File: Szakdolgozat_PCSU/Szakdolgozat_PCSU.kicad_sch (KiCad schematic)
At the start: 66 parts, among them IC1 DRV8244SQDGQRQ1, IC2 TPS54628DDAR, IC3 DRV8244SQDGQRQ1, IC4 LTC4365ITS8-1#TRPBF, J1 MOTOR1_OUT, J2 M1_SPI, J3 M1_CTRL, J4 MOTOR2_OUT, J5 M2_SPI, J6 M2_CTRL, J7 5V_CON, J8 BAT_CON, Q1 STP130N6F7, Q2 STP130N6F7

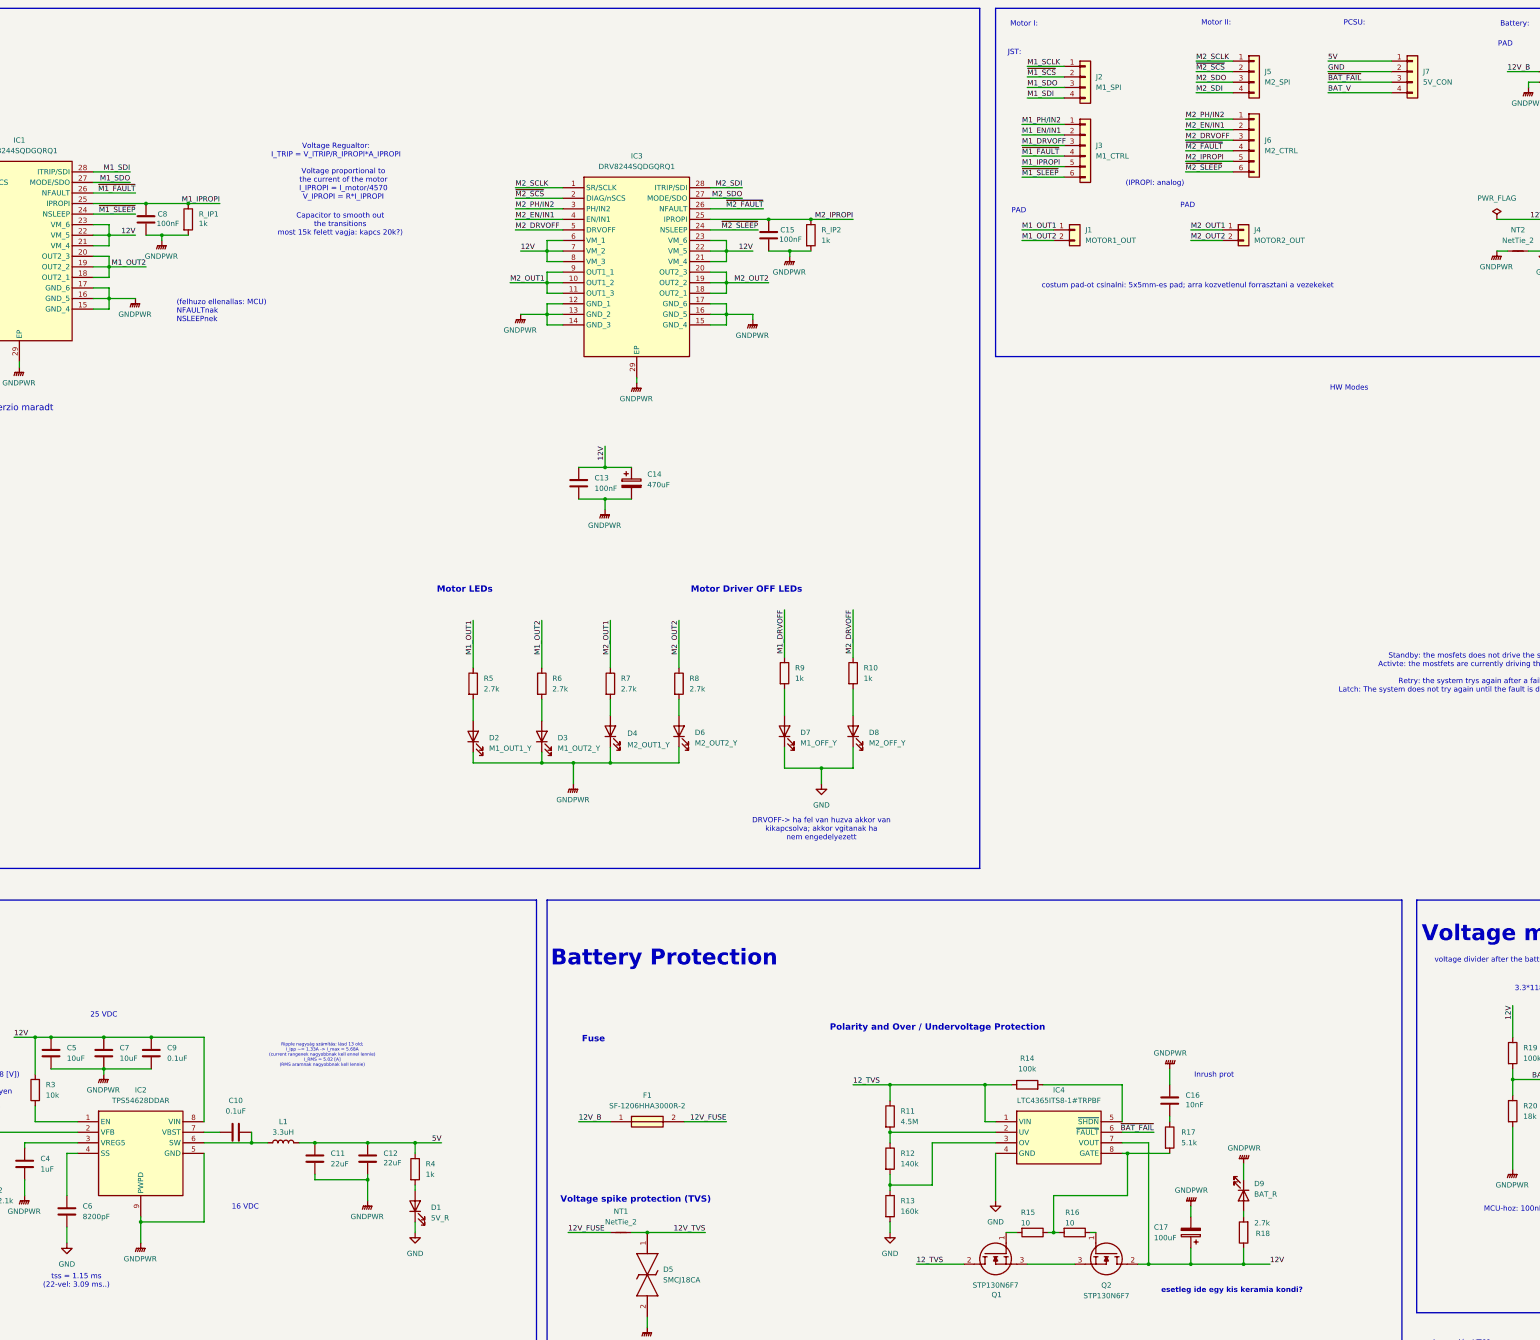
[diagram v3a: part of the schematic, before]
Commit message: Update PCSU PCB routing, copper pours and vias
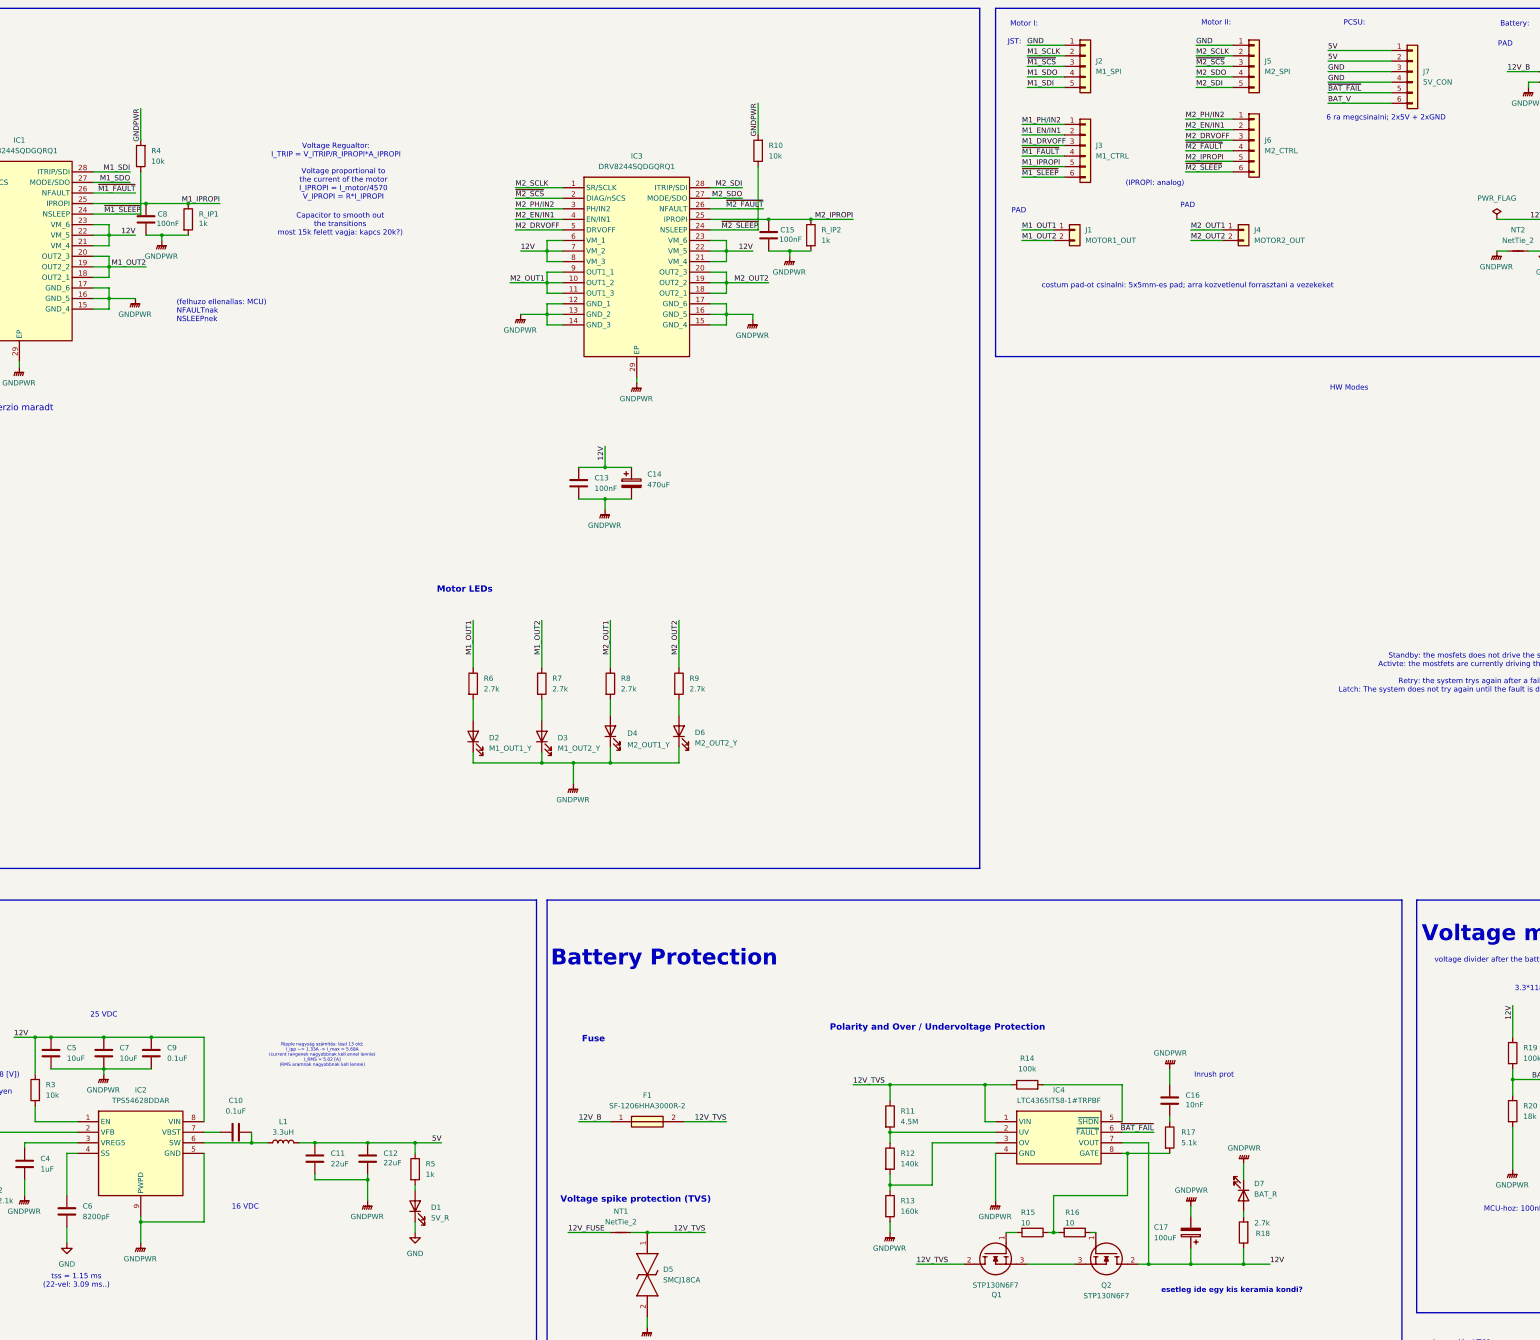
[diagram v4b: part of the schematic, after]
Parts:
- removed D7: M1_OFF_Y, LED_SMD:LED_0603_1608Metric_Pad1.05x0.95mm_HandSolder, symbol Device:LED
- removed D8: M2_OFF_Y, LED_SMD:LED_0603_1608Metric_Pad1.05x0.95mm_HandSolder, symbol Device:LED
- removed R9: 1k, Resistor_SMD:R_0603_1608Metric_Pad0.98x0.95mm_HandSolder, symbol Device:R
- added R4: 10k, Resistor_SMD:R_0603_1608Metric_Pad0.98x0.95mm_HandSolder, symbol Device:R
- C16: footprint Capacitor_SMD:C_1206_3216Metric_Pad1.33x1.80mm_HandSolder -> Capacitor_SMD:C_0603_1608Metric_Pad1.08x0.95mm_HandSolder
- J2, J5: footprint Connector_JST:JST_XH_S4B-XH-A-1_1x04_P2.50mm_Horizontal -> Connector_JST:JST_XH_S5B-XH-A-1_1x05_P2.50mm_Horizontal; symbol Connector_Generic:Conn_01x04 -> Connector_Generic:Conn_01x05
- J7: footprint Connector_JST:JST_XH_S4B-XH-A-1_1x04_P2.50mm_Horizontal -> Connector_JST:JST_XH_S6B-XH-A-1_1x06_P2.50mm_Horizontal; symbol Connector_Generic:Conn_01x04 -> Connector_Generic:Conn_01x06
- NT2: footprint (none) -> NetTie:Untitled; now in the parts list
- R10: value 1k -> 10k
- renumbered D9 to D7, R4 to R5, R5 to R6, R6 to R7, R7 to R8, R8 to R9
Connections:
- net 12_TVS is gone; now on net 12V_TVS: IC4.1 (VIN), Q1.2 (D), R11.1, R14.1
- net 12V_FUSE: no longer F1.2
- net 12V_TVS: now also F1.2
- net 5V: now also J7.2 (Pin_2)
- net BAT_V: now also J7.6 (Pin_6); no longer J7.4 (Pin_4)
- net GND: now also J2.1 (Pin_1), J5.1 (Pin_1), J7.3 (Pin_3), J7.4 (Pin_4); no longer IC4.4 (GND), J7.2 (Pin_2), R13.2
- net GNDPWR: now also IC4.4 (GND), R10.2, R13.2, R4.2
- net M1_SCLK: now also J2.2 (Pin_2); no longer J2.1 (Pin_1)
- net M1_SDI: now also J2.5 (Pin_5); no longer J2.4 (Pin_4)
- net M1_SDO: now also J2.4 (Pin_4); no longer J2.3 (Pin_3)
- net M2_DRVOFF: no longer R10.1
- net M2_SCLK: now also J5.2 (Pin_2); no longer J5.1 (Pin_1)
- net M2_SDI: now also J5.5 (Pin_5); no longer J5.4 (Pin_4)
- net M2_SDO: now also J5.4 (Pin_4); no longer J5.3 (Pin_3)
- net ~{BAT_FAIL}: now also J7.5 (Pin_5); no longer J7.3 (Pin_3)
- net ~{M1_SCS}: now also J2.3 (Pin_3); no longer J2.2 (Pin_2)
- net ~{M1_SLEEP}: now also R4.1
- net ~{M2_SCS}: now also J5.3 (Pin_3); no longer J5.2 (Pin_2)
- net ~{M2_SLEEP}: now also R10.1
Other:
- note added: "6 ra megcsinalni; 2x5V + 2xGND"
- note removed: "DRVOFF-> ha fel van huzva akkor van kikapcsolva; akkor vgitanak ha nem engedelyezett"
- note removed: "Motor Driver OFF LEDs"

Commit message: CU es PCSU Rev A finished + Production Files
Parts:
- removed NT1: NetTie_2, symbol Device:NetTie_2
- C16: Link https://hu.mouser.com/en/ProductDetail/Murata-Electronics/G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 -> https://hu.mouser.com/ProductDetail/Murata-Electronics/GRM1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
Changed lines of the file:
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@@
 	)
 	(junction
-		(at 247.65 309.88)
-		(diameter 0)
-		(color 0 0 0 0)
-	)
-	(junction
 		(at 223.52 73.66)
 		(diameter 0)
@@
 	(wire
 		(pts
-			(xy 247.65 309.88) (xy 261.62 309.88)
-		)
-		(stroke
-			(width 0)
-			(type default)
-		)
-	)
-	(wire
-		(pts
 			(xy 361.95 290.83) (xy 363.22 290.83)
 		)
@@
 	(wire
 		(pts
-			(xy 228.6 309.88) (xy 238.76 309.88)
-		)
-		(stroke
-			(width 0)
-			(type default)
-		)
-	)
-	(wire
-		(pts
 			(xy 266.7 73.66) (xy 266.7 76.2)
 		)
@@
 	(wire
 		(pts
-			(xy 243.84 309.88) (xy 247.65 309.88)
-		)
-		(stroke
-			(width 0)
-			(type default)
-		)
-	)
-	(wire
-		(pts
 			(xy 306.07 307.34) (xy 306.07 309.88)
 		)
@@
 		)
 	)
-	(label "12V_TVS"
-		(at 261.62 309.88 180)
-		(effects
-			(font
-				(size 1.27 1.27)
-			)
-			(justify right bottom)
-		)
-	)
 	(label "M1_EN{slash}IN1"
 		(at 337.82 45.72 0)
@@
 		)
 	)
-	(label "12V_FUSE"
-		(at 228.6 309.88 0)
-		(effects
-			(font
-				(size 1.27 1.27)
-			)
-			(justify left bottom)
-		)
-	)
 	(label "M1_OUT2"
 		(at 337.82 71.12 0)
@@
 	)
 	(symbol
-		(lib_id "Device:NetTie_2")
-		(at 241.3 309.88 0)
-		(unit 1)
-		(body_style 1)
-		(exclude_from_sim no)
-		(in_bom no)
-		(on_board yes)
-		(in_pos_files yes)
-		(dnp no)
-		(fields_autoplaced yes)
-		(property "Reference" "NT1"
-			(at 241.3 304.8 0)
-			(show_name no)
-			(do_not_autoplace no)
-			(effects
-				(font
-					(size 1.27 1.27)
-				)
-			)
-		)
-		(property "Value" "NetTie_2"
-			(at 241.3 307.34 0)
-			(show_name no)
-			(do_not_autoplace no)
-			(effects
-				(font
-					(size 1.27 1.27)
-				)
-			)
-		)
-		(property "Footprint" ""
-			(at 241.3 309.88 0)
-			(hide yes)
-			(show_name no)
-			(do_not_autoplace no)
-			(effects
-				(font
-					(size 1.27 1.27)
-				)
-			)
-		)
-		(property "Datasheet" ""
-			(at 241.3 309.88 0)
-			(hide yes)
-			(show_name no)
-			(do_not_autoplace no)
-			(effects
-				(font
-					(size 1.27 1.27)
-				)
-			)
-		)
-		(property "Description" "Net tie, 2 pins"
-			(at 241.3 309.88 0)
-			(hide yes)
-			(show_name no)
-			(do_not_autoplace no)
-			(effects
-				(font
-					(size 1.27 1.27)
-				)
-			)
-		)
-		(pin "2"
-		)
-		(pin "1"
-		)
-		(instances
-			(project "Szakdolgozat_PCSU"
-				(path "/7dedd975-a421-4fd7-bcb8-a9f9c9e19d4a"
-					(reference "NT1")
-					(unit 1)
-				)
-			)
-		)
-	)
-	(symbol
 		(lib_id "power:GNDPWR")
 		(at 459.74 34.29 0)
@@
 			)
 		)
-		(property "Datasheet" "https://hu.mouser.com/datasheet/3/76/4/GRM319R61C226KE15_04A.pdf"
+		(property "Datasheet" "https://search.murata.co.jp/Ceramy/image/img/A01X/G101/ENG/GRM188R71H103KA01-01.pdf"
 			(at 373.38 278.13 0)
 			(hide yes)
@@
 			)
 		)
-		(property "Link" "https://hu.mouser.com/en/ProductDetail/Murata-Electronics/GRM319R61C226KE15D?qs=eeBpzGFlv%252B%252BgKZpdhYn80g%3D%3D"
+		(property "Link" "https://hu.mouser.com/ProductDetail/Murata-Electronics/GRM188R71H103KA01D"
 			(at 373.38 278.13 0)
 			(hide yes)
@@
 	)
 	(embedded_fonts no)
+(symbol
+		(lib_id "power:PWR_FLAG")
+		(at 64.77 139.7 0)
+		(unit 1)
+		(body_style 1)
+		(exclude_from_sim no)
+		(in_bom yes)
+		(on_board yes)
+		(in_pos_files yes)
+		(dnp no)
+		(fields_autoplaced yes)
+		(property "Reference" "#FLG02"
+			(at 64.77 137.795 0)
+			(hide yes)
+			(show_name no)
+			(do_not_autoplace no)
+			(effects
+				(font
+					(size 1.27 1.27)
+				)
+			)
+		)
+		(property "Value" "PWR_FLAG"
+			(at 64.77 134.62 0)
+			(show_name no)
+			(do_not_autoplace no)
+			(effects
+				(font
+					(size 1.27 1.27)
+				)
+			)
+		)
+		(property "Footprint" ""
+			(at 64.77 139.7 0)
+			(hide yes)
+			(show_name no)
+			(do_not_autoplace no)
+			(effects
+				(font
+					(size 1.27 1.27)
+				)
+			)
+		)
+		(property "Datasheet" ""
+			(at 64.77 139.7 0)
+			(hide yes)
+			(show_name no)
+			(do_not_autoplace no)
+			(effects
+				(font
+					(size 1.27 1.27)
+				)
+			)
+		)
+		(property "Description" "Special symbol for telling ERC where power comes from"
+			(at 64.77 139.7 0)
+			(hide yes)
+			(show_name no)
+			(do_not_autoplace no)
+			(effects
+				(font
+					(size 1.27 1.27)
+				)
+			)
+		)
+		(pin "1"
+		)
+		(instances
+			(project "Szakdolgozat_PCSU"
+				(path "/7dedd975-a421-4fd7-bcb8-a9f9c9e19d4a"
+					(reference "#FLG02")
+					(unit 1)
+				)
+			)
+		)
+	)
+(symbol
+		(lib_id "power:PWR_FLAG")
+		(at 87.63 309.88 0)
+		(unit 1)
+		(body_style 1)
+		(exclude_from_sim no)
+		(in_bom yes)
+		(on_board yes)
+		(in_pos_files yes)
+		(dnp no)
+		(fields_autoplaced yes)
+		(property "Reference" "#FLG03"
+			(at 87.63 307.975 0)
+			(hide yes)
+			(show_name no)
+			(do_not_autoplace no)
+			(effects
+				(font
+					(size 1.27 1.27)
+				)
+			)
+		)
+		(property "Value" "PWR_FLAG"
+			(at 87.63 304.8 0)
+			(show_name no)
+			(do_not_autoplace no)
+			(effects
+				(font
+					(size 1.27 1.27)
+				)
+			)
+		)
+		(property "Footprint" ""
+			(at 87.63 309.88 0)
+			(hide yes)
+			(show_name no)
+			(do_not_autoplace no)
+			(effects
+				(font
+					(size 1.27 1.27)
+				)
+			)
+		)
+		(property "Datasheet" ""
+			(at 87.63 309.88 0)
+			(hide yes)
+			(show_name no)
+			(do_not_autoplace no)
+			(effects
+				(font
+					(size 1.27 1.27)
+				)
+			)
+		)
+		(property "Description" "Special symbol for telling ERC where power comes from"
+			(at 87.63 309.88 0)
+			(hide yes)
+			(show_name no)
+			(do_not_autoplace no)
+			(effects
+				(font
+					(size 1.27 1.27)
+				)
+			)
+		)
+		(pin "1"
+		)
+		(instances
+			(project "Szakdolgozat_PCSU"
+				(path "/7dedd975-a421-4fd7-bcb8-a9f9c9e19d4a"
+					(reference "#FLG03")
+					(unit 1)
+				)
+			)
+		)
+	)
+(wire
+		(pts
+			(xy 247.65 309.88) (xy 261.62 309.88)
+		)
+		(stroke
+			(width 0)
+			(type default)
+		)
+	)
+(label "12V_TVS"
+		(at 261.62 309.88 180)
+		(effects
+			(font
+				(size 1.27 1.27)
+			)
+			(justify right bottom)
+		)
+	)
 )
